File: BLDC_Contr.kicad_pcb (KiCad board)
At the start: 4 copper layers, 100 parts, among them J1 XT60, J10 PH, J2 MR60, J3 Conn_ARM_SWD_TagConnect_TC2030, J4 PH, J5 PH, J6 PH, J7 PH, J8 PH, J9 PIN, Q1 CSD18540Q5B, Q2 CSD18540Q5B, Q3 CSD18540Q5B, Q4 CSD18540Q5B, Q5 CSD18540Q5B, Q6 CSD18540Q5B, U1 STM32G431CBU6, U2 DRV8323RSRGZR, U3 AMS1117-3.3, Y1 Crystal_16Mhz

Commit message: add PCB layouts
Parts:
- removed the C2 at (24.9, 29.7)
- removed the C23 at (27.9, 54.7)
- removed the J2 at (63.8, 60.2)
- added H5: MountingHole_Pad_MP, MountingHole:MountingHole_2.5mm_Pad_Via, F.Cu at (156.7, 30.6)
- added H6: MountingHole_Pad_MP, MountingHole:MountingHole_2.5mm_Pad_Via, F.Cu at (141.4, 30.6)
- added H7: MountingHole_Pad_MP, MountingHole:MountingHole_2.5mm_Pad_Via, F.Cu at (126.2, 30.6)
- C18: renamed from C19; footprint Capacitor_SMD:C_0603_1608Metric -> Capacitor_SMD:C_1210_3225Metric
- C19: renamed from C20; footprint Capacitor_SMD:C_0603_1608Metric -> Capacitor_SMD:C_1210_3225Metric
- D10, D13, D6, D8: footprint Package_TO_SOT_SMD:SOT-143 -> Diode_SMD:Nexperia_DSN1608-2_1.6x0.8mm
- D11: footprint Diode_SMD:D_0201_0603Metric -> Package_TO_SOT_SMD:SOT-23
- D12, D4, D5, D7, D9: footprint Package_TO_SOT_SMD:SOT-23-3 -> Package_TO_SOT_SMD:SOT-523
- J10: footprint Connector_JST:JST_PH_S4B-PH-K_1x04_P2.00mm_Horizontal -> Connector_JST:JST_PH_S5B-PH-K_1x05_P2.00mm_Horizontal
- J2: renamed from J3; footprint Connector:Tag-Connect_TC2030-IDC-FP_2x03_P1.27mm_Vertical -> Connector:Tag-Connect_TC2030-IDC-NL_2x03_P1.27mm_Vertical
- R21, R22: value 0 -> 56
- U5: moved to B.Cu
- moved C10 140.6 mm to (166.2, 62.6), turned to 90 degrees
- moved C35 140.3 mm to (163.5, 48.0), turned to -90 degrees
- moved C34 133.9 mm to (158.4, 48.0), turned to -90 degrees
- moved C9 129.3 mm to (154.5, 60.6), turned to 90 degrees
- moved C24 124.5 mm to (152.8, 75.9), turned to 90 degrees
- moved C21 121.4 mm to (148.6, 62.6), turned to 180 degrees
- moved C20 117.0 mm to (144.8, 71.5)
- moved H2 116.2 mm to (170.0, 30.0)
- moved C33 115.3 mm to (140.7, 48.0), turned to -90 degrees
- moved D4 115.2 mm to (162.3, 76.1), turned to 90 degrees
- moved C19 113.0 mm to (141.3, 66.7)
- moved C18 112.6 mm to (141.3, 62.9)
- moved C25 111.5 mm to (140.0, 76.1), turned to 90 degrees
- moved D5 111.4 mm to (158.8, 76.1), turned to 90 degrees
- moved C32 109.2 mm to (135.6, 48.0), turned to -90 degrees
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- renumbered C11 to C10, C12 to C11, C13 to C12, C14 to C13, C15 to C14, C16 to C15, C17 to C16, C18 to C17, C3 to C2, C21 to C20, C22 to C21, C24 to C23, C25 to C24, C26 to C25, C27 to C26, C28 to C27, C29 to C28, C30 to C29, C4 to C3, C36 to C30, C5 to C4, C6 to C5, C7 to C6, C8 to C7, C9 to C8, C10 to C9, J4 to J3, J5 to J4, J6 to J5, J7 to J6, J8 to J7, J9 to J8, R16 to R13, R13 to R14, R14 to R15, R15 to R16
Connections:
- C17 pad 1: +3.3V -> +3.3VA
- D10 pad 1: GND -> +3.3V
- D10 pad 2: +3.3V -> GND
- D11 pad 1: /CAN_H_C -> /CAN_L_C
- D11 pad 2: /CAN_L_C -> /CAN_H_C
- D12 pad 1: /AMT_B_C -> /AMT_A_C
- D12 pad 2: /AMT_A_C -> /AMT_B_C
- D13 pad 1: GND -> +5V
- D13 pad 2: +5V -> GND
- D4 pad 1: /SPI1_NCS_C -> /SPI1_MOSI_C
- D4 pad 2: /SPI1_MOSI_C -> /SPI1_NCS_C
- D5 pad 1: /SPI1_MISO_C -> /SPI1_SCK_C
- D5 pad 2: /SPI1_SCK_C -> /SPI1_MISO_C
- D6 pad 1: GND -> +3.3V
- D6 pad 2: +3.3V -> GND
- D8 pad 1: GND -> +3.3V
- D8 pad 2: +3.3V -> GND
- J6 pad 1: /CAN_H_C -> /CAN_L_C
- J6 pad 2: /CAN_L_C -> /CAN_H_C
- J7 pad 1: /CAN_H_C -> /CAN_L_C
- J7 pad 2: /CAN_L_C -> /CAN_H_C
- U2 pad 26: +3.3V -> +3.3VA
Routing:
- net GND: track 0.00 -> 110.4 mm, vias 0 -> 6
- net +5V: track 0.00 -> 65.5 mm, vias 0 -> 4
- net +3.3V: track 0.00 -> 63.2 mm, vias 0 -> 5
- net GHA: track 0.00 -> 46.8 mm
- net SHA: track 0.00 -> 44.8 mm
- net SHB: track 0.00 -> 40.0 mm
- net GLA: track 0.00 -> 39.3 mm
- net GLB: track 0.00 -> 39.0 mm
- net SPA: track 0.00 -> 37.8 mm
- net +BATT: track 0.00 -> 36.9 mm, vias 0 -> 1
- net /CAN_L_C: track 0.00 -> 36.6 mm, vias 0 -> 2
- net /CAN_H_C: track 0.00 -> 34.4 mm, vias 0 -> 2
- net GHB: track 0.00 -> 33.3 mm
- net GHC: track 0.00 -> 29.4 mm
- net SPB: track 0.00 -> 29.1 mm
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- added copper zone on F.Cu, net +5V
- added copper zone on F.Cu, net +BATT
- added copper zone on In2.Cu, net +BATT
- added copper zone on F.Cu, net SHA
- added copper zone on In2.Cu, net SHA
- added copper zone on F.Cu, net SHB
- added copper zone on In2.Cu, net SHB
- added copper zone on F.Cu, net SHC
- added copper zone on In2.Cu, net SHC
- added copper zone on F.Cu, net SPA
- added copper zone on F.Cu, net SPB
- added copper zone on F.Cu, net SPC
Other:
- board outline added: 90 x 65 mm

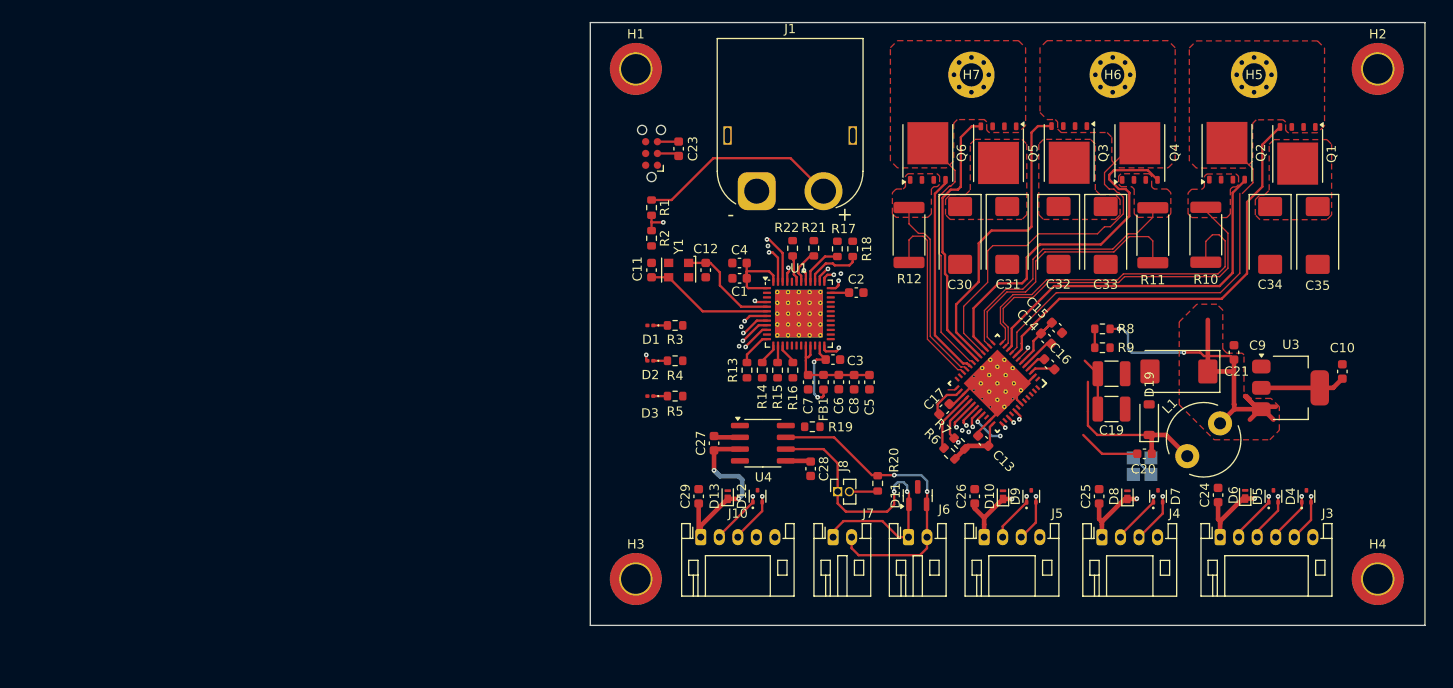
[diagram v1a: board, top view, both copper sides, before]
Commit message: add wiring. changed communication of spi on drv8323 from spi2 to spi1 for better wiring.
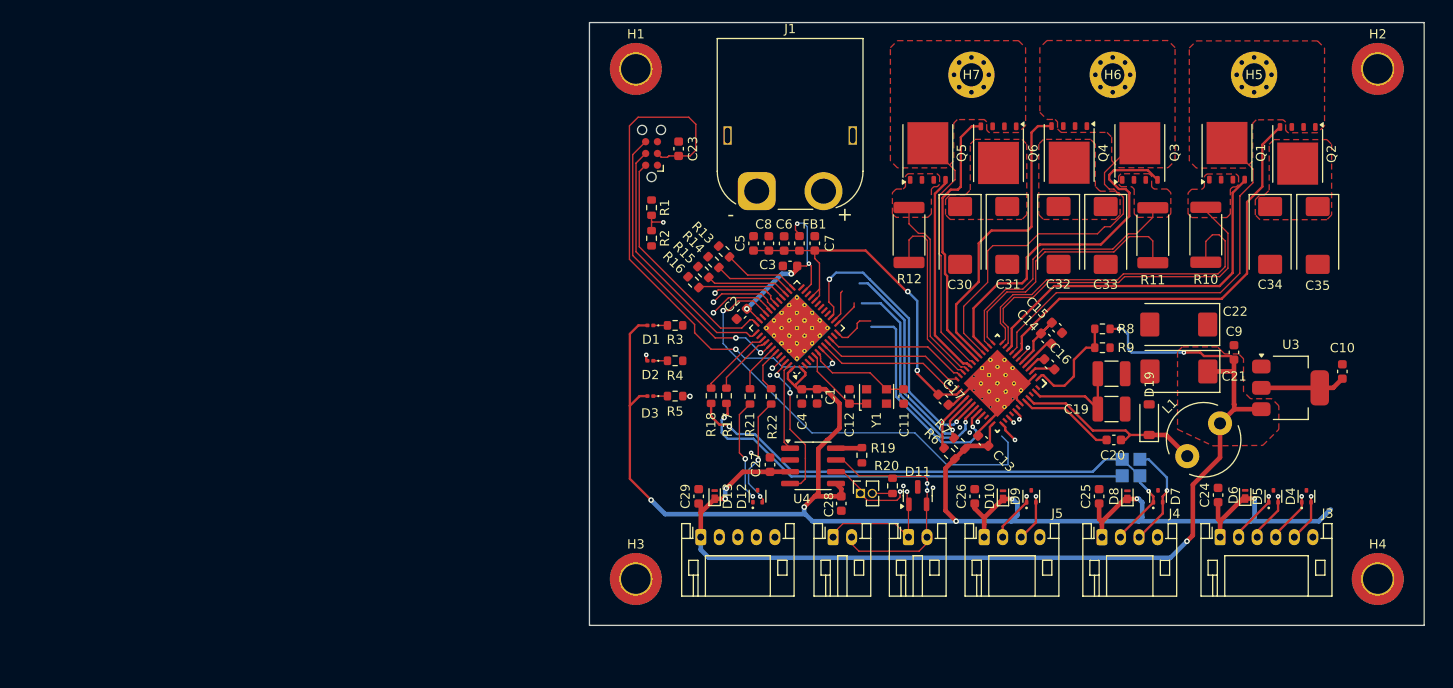
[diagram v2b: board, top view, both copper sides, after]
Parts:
- added C22: 15u, Capacitor_Tantalum_SMD:CP_EIA-7343-31_Kemet-D, F.Cu at (148.5, 57.6)
- R10, R11, R12: value 3m -> 1m
- moved C11 30.4 mm to (118.9, 65.3), turned to -90 degrees
- moved Y1 25.3 mm to (116.0, 65.3), turned to 90 degrees
- moved R18 22.0 mm to (98.1, 65.2), turned to -90 degrees
- moved C12 20.6 mm to (113.0, 65.3), turned to 90 degrees
- moved R17 19.8 mm to (99.8, 65.2), turned to -90 degrees
- moved C5 19.5 mm to (102.7, 48.8), turned to 90 degrees
- moved C8 17.6 mm to (104.3, 48.8), turned to 90 degrees
- moved R21 17.4 mm to (102.3, 65.3), turned to -90 degrees
- moved R22 16.1 mm to (104.6, 65.3), turned to -90 degrees
- moved C6 16.1 mm to (106.0, 48.8), turned to 90 degrees
- moved C4 15.9 mm to (107.9, 65.3), turned to -90 degrees
- moved C1 15.2 mm to (109.5, 65.3), turned to -90 degrees
- moved FB1 15.2 mm to (107.6, 48.8), turned to -90 degrees
- moved C7 15.0 mm to (109.3, 48.8), turned to 90 degrees
- moved R16 14.3 mm to (96.2, 53.0), turned to -45 degrees
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- renumbered Q2 to Q1, Q1 to Q2, Q4 to Q3, Q3 to Q4, Q6 to Q5, Q5 to Q6
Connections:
- H5 pad 1: SHA -> (no net)
- H6 pad 1: SHB -> (no net)
- H7 pad 1: SHC -> (no net)
- R13 pad 2: SP1_NCS -> SP2_NCS
- R14 pad 1: SP1_SCK -> SP2_SCK
- R15 pad 1: SP1_MISO -> SP2_MISO
- R16 pad 2: SP1_MOSI -> SP2_MOSI
- R7 pad 2: SP2_MISO -> SP1_MISO
- U2 pad 29: SP2_MISO -> SP1_MISO
- U2 pad 30: SP2_MOSI -> SP1_MOSI
- U2 pad 31: SP2_SCK -> SP1_SCK
- U2 pad 32: SP2_NCS -> SP1_NCS
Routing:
- net +3.3V: track 63.2 -> 205.0 mm, vias 5 -> 10
- net NRST: track 5.04 -> 59.5 mm, vias 1 -> 2
- net +5V: track 65.5 -> 114.2 mm, vias 4 -> 5
- net Net-(U5-Rx_In): track 0.00 -> 48.6 mm, vias 0 -> 1
- net Net-(U5-Tx_In): track 0.00 -> 48.3 mm, vias 0 -> 1
- net MOTOR_HiZ: track 4.17 -> 49.8 mm
- net SWO: track 1.32 -> 32.3 mm, vias 1 -> 2
- net SP1_MOSI: track 2.29 -> 32.6 mm, vias 0 -> 2
- net SP1_MISO: track 1.85 -> 30.2 mm, vias 0 -> 1
- net SWCLK: track 1.58 -> 27.9 mm, vias 1 -> 0
- net SP1_SCK: track 2.33 -> 28.0 mm, vias 0 -> 1
- net SP1_NCS: track 3.70 -> 29.2 mm, vias 0 -> 1
- net +3.3VA: track 15.8 -> 40.6 mm, vias 0 -> 2
- net SWDIO: track 1.47 -> 25.9 mm, vias 1 -> 0
- net +BATT: track 36.9 -> 20.7 mm
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
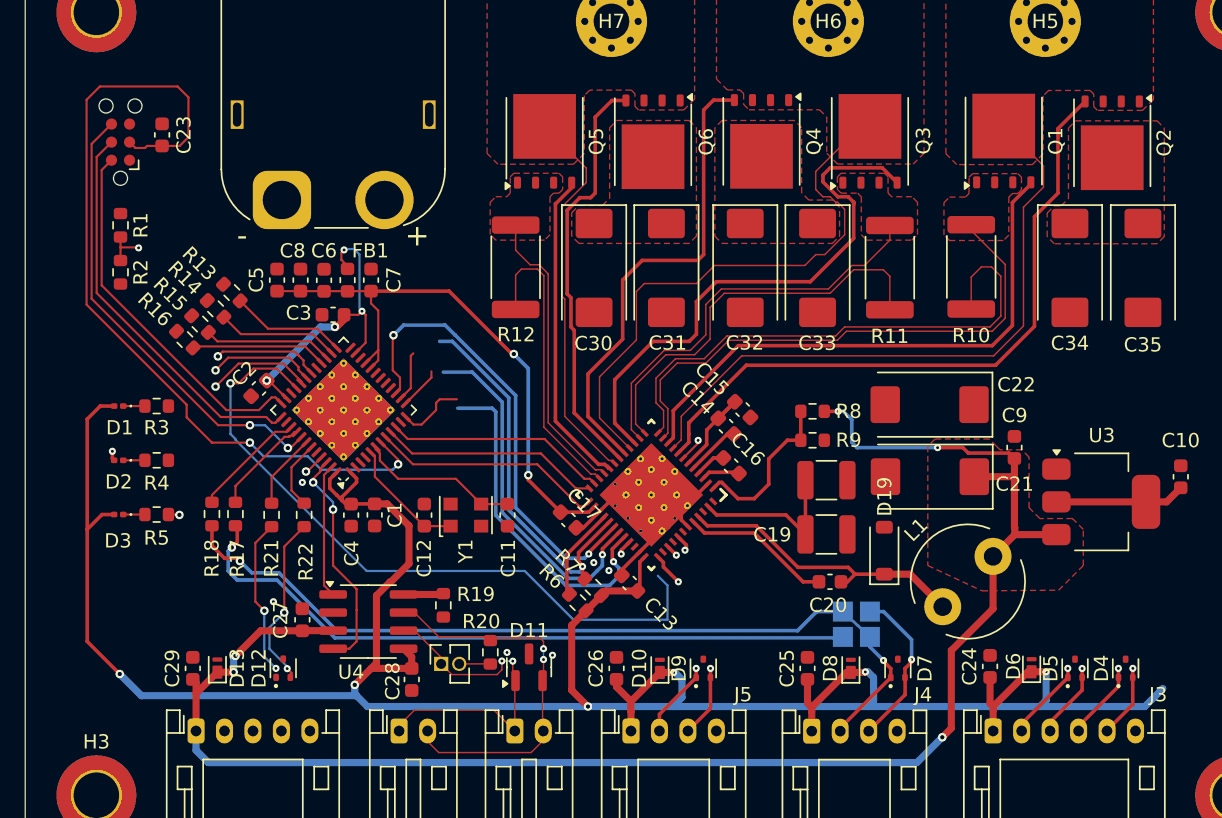
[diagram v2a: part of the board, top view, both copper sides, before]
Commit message: added most wiring, not erc checked. changed pinouts on connectors for easier wiring
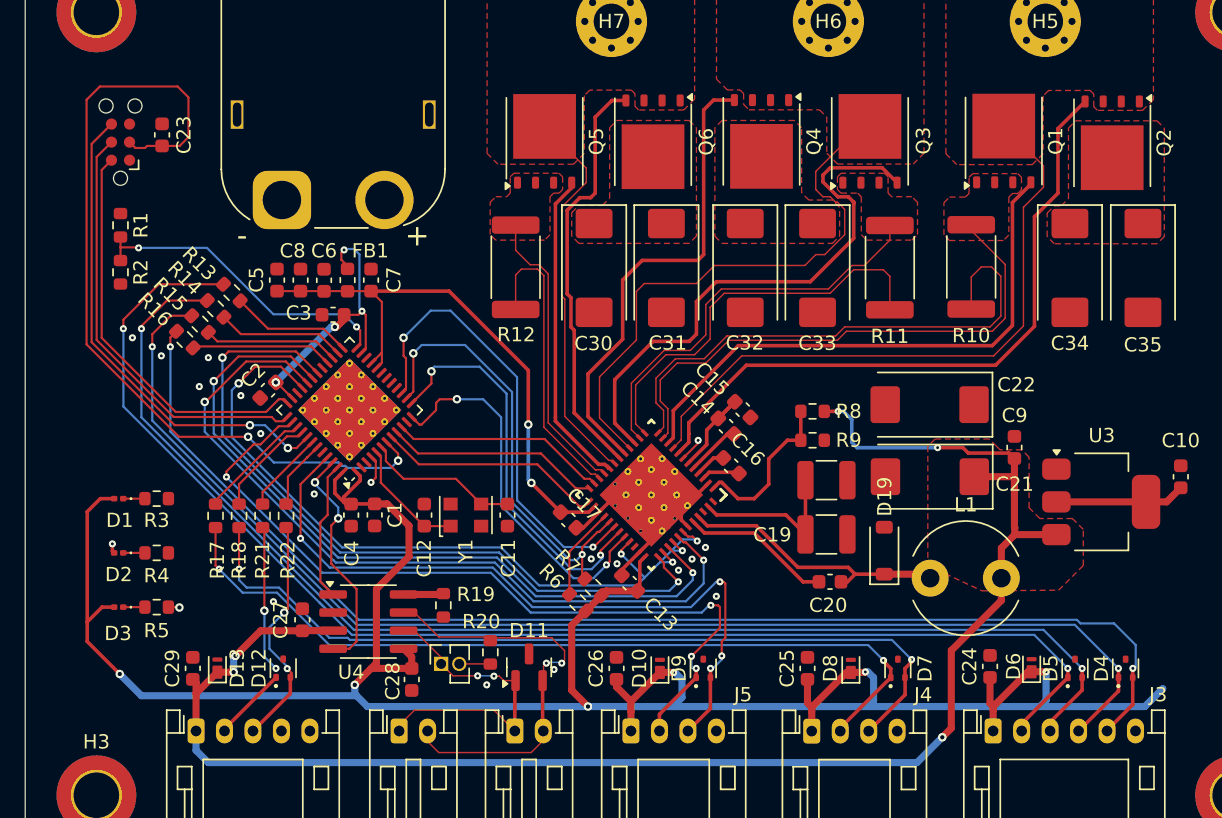
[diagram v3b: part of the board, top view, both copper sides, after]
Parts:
- removed U5: ~, poka-yoke_rxtx:poka-yoke_rxtx
- moved D3 6.51 mm to (91.6, 71.8)
- moved D1 6.51 mm to (91.6, 64.2)
- moved D2 6.50 mm to (91.6, 68.0)
- moved R3 6.50 mm to (94.2, 64.2)
- moved R4 6.50 mm to (94.2, 68.0)
- moved R5 6.50 mm to (94.2, 71.8)
- moved L1 2.19 mm to (148.6, 69.8), turned to 0 degrees
- moved R18 1.91 mm to (100.0, 65.4)
- moved R17 1.40 mm to (98.4, 65.4)
- moved R22 1.27 mm to (103.3, 65.4)
- moved C2 0.65 mm to (102.1, 56.5)
- moved R21 0.64 mm to (101.7, 65.4)
- moved U1 0.42 mm to (107.8, 57.9)
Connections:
- D4 pad 1: /SPI1_MOSI_C -> /SPI1_MISO_C
- D4 pad 2: /SPI1_NCS_C -> /SPI1_SCK_C
- D5 pad 1: /SPI1_SCK_C -> /SPI1_NCS_C
- D5 pad 2: /SPI1_MISO_C -> /SPI1_MOSI_C
- D7 pad 1: /UART_TX_C -> /UART_RX_C
- D7 pad 2: /UART_RX_C -> /UART_TX_C
- D9 pad 1: I2C_SDA -> I2C_SCL
- D9 pad 2: I2C_SCL -> I2C_SDA
- J3 pad 2: /SPI1_SCK_C -> /SPI1_NCS_C
- J3 pad 3: /SPI1_MISO_C -> /SPI1_MOSI_C
- J3 pad 4: /SPI1_MOSI_C -> /SPI1_MISO_C
- J3 pad 5: /SPI1_NCS_C -> /SPI1_SCK_C
- J4 pad 2: /UART_TX_C -> /UART_RX_C
- J4 pad 3: /UART_RX_C -> /UART_TX_C
- J5 pad 2: I2C_SDA -> I2C_SCL
- J5 pad 3: I2C_SCL -> I2C_SDA
- R14 pad 1: SP2_SCK -> SP2_MOSI
- R14 pad 2: /SPI1_SCK_C -> /SPI1_MOSI_C
- R16 pad 1: /SPI1_MOSI_C -> /SPI1_SCK_C
- R16 pad 2: SP2_MOSI -> SP2_SCK
- R17 pad 1: RX -> TX
- R17 pad 2: Net-(U5-Rx_In) -> /UART_RX_C
- R18 pad 1: TX -> RX
- R18 pad 2: Net-(U5-Tx_In) -> /UART_TX_C
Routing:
- net /SPI1_NCS_C: track 5.15 -> 95.0 mm, vias 1 -> 2
- net /SPI1_MISO_C: track 5.33 -> 90.4 mm, vias 1 -> 2
- net /SPI1_MOSI_C: track 5.56 -> 90.5 mm, vias 1 -> 2
- net /SPI1_SCK_C: track 5.75 -> 88.1 mm, vias 1 -> 2
- net I2C_SCL: track 5.06 -> 56.3 mm, vias 1 -> 4
- net /UART_TX_C: track 8.29 -> 59.5 mm, vias 1 -> 2
- net Net-(U5-Rx_In): track 48.6 -> 0.00 mm, vias 1 -> 0
- net Net-(U5-Tx_In): track 48.3 -> 0.00 mm, vias 1 -> 0
- net /UART_RX_C: track 11.4 -> 59.0 mm, vias 1 -> 2
- net INHC: track 8.56 -> 55.7 mm
- net INHB: track 8.31 -> 53.9 mm
- net I2C_SDA: track 7.10 -> 50.7 mm, vias 2 -> 4
- net INHA: track 9.99 -> 52.1 mm
- net VIN_DIVIDER: track 2.94 -> 22.2 mm, vias 1 -> 2
- net +3.3V: track 205.0 -> 196.7 mm
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
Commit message: wired every component, ground poured doing erc (not done yet)
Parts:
- moved C9 9.82 mm to (158.6, 69.5), turned to 0 degrees
- moved C10 7.66 mm to (159.1, 59.7), turned to 180 degrees
- moved C3 4.08 mm to (110.2, 53.2), turned to -45 degrees
- moved D6 3.22 mm to (152.5, 76.2)
- moved C25 3.10 mm to (143.0, 75.7)
- moved D8 2.84 mm to (140.2, 76.2)
- moved C24 2.65 mm to (155.4, 75.7)
- moved C26 0.37 mm to (126.5, 75.7)
- moved U3 0.16 mm to (160.6, 64.5)
- moved D10 0.06 mm to (129.6, 76.2)
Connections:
- H5 pad 1: (no net) -> SHA
- H6 pad 1: (no net) -> SHB
- H7 pad 1: (no net) -> SHC
- U2 pad V: (no net) -> GND
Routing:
- net USER_LED: track 2.71 -> 44.9 mm
- net +3.3V: track 196.7 -> 234.4 mm, vias 10 -> 12
- net NFAULT_PRE: track 7.24 -> 40.2 mm, vias 1 -> 2
- net GND: track 105.6 -> 107.6 mm, vias 16 -> 26
- net +5V: track 114.2 -> 116.0 mm
- net /SPI1_MOSI_C: track 90.5 -> 91.8 mm
- net /SPI1_NCS_C: track 95.0 -> 94.1 mm
- net +3.3VA: track 40.3 -> 41.1 mm
- net I2C_SCL: track 56.3 -> 57.0 mm
- net /SPI1_SCK_C: track 88.1 -> 88.7 mm
- net NRST: track 60.2 -> 60.8 mm
- added copper zone on F.Cu, net +3.3V
- added copper zone on B.Cu, net +BATT
- added copper zone on In1.Cu, net +BATT
- added copper zone on B.Cu, net GND
- added copper zone on F.Cu, net GND
- added copper zone on In1.Cu, net GND
- added copper zone on In2.Cu, net GND
